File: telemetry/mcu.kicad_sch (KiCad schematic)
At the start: 6 parts, among them J6 ZIO_CN8, J7 ZIO_CN9, J8 ZIO_CN7, J9 ZIO_CN10

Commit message: Updated MCU file to be Nucleo-446RE
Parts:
- removed J6: ZIO_CN8, Connector_PinSocket_2.54mm:PinSocket_2x08_P2.54mm_Vertical, symbol Connector_Generic:Conn_02x08_Odd_Even
- removed J8: ZIO_CN7, Connector_PinSocket_2.54mm:PinSocket_2x10_P2.54mm_Vertical, symbol Connector_Generic:Conn_02x10_Odd_Even
- removed R4, R5: 10k, Resistor_SMD:R_0805_2012Metric_Pad1.20x1.40mm_HandSolder, symbol Device:R_Small
- J7: value ZIO_CN9 -> CN7; symbol Connector_Generic:Conn_02x15_Odd_Even -> Connector_Generic:Conn_02x19_Odd_Even
- J9: value ZIO_CN10 -> CN10; footprint Connector_PinSocket_2.54mm:PinSocket_2x17_P2.54mm_Vertical -> Connector_PinSocket_2.54mm:PinSocket_2x19_P2.54mm_Vertical; symbol Connector_Generic:Conn_02x17_Odd_Even -> Connector_Generic:Conn_02x19_Odd_Even
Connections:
- net APPS_1: no longer names the net of J7.2 (Pin_2)
- net APPS_2: no longer names the net of J7.6 (Pin_6)
- net BPS: no longer names the net of J7.4 (Pin_4)
- net CAN1_RX: no longer names the net of J7.26 (Pin_26)
- net CAN1_TX: no longer names the net of J7.28 (Pin_28)
- net CAN2_TX: no longer names the net of J9.14 (Pin_14)
- net DRS: no longer names the net of J9.30 (Pin_30)
- removed net GND: J7.24 (Pin_24), J9.18 (Pin_18), J9.21 (Pin_21), J9.28 (Pin_28), J9.6 (Pin_6)
- net GPIO_IN_1: no longer names the net of J7.8 (Pin_8)
- net GPIO_IN_2: no longer names the net of J7.10 (Pin_10)
- net GPIO_OUT_1: no longer names the net of J9.5 (Pin_5)
- net GPIO_OUT_2: no longer names the net of J9.7 (Pin_7)
- net GPIO_OUT_3: no longer names the net of J9.9 (Pin_9)
- net RTDI: no longer names the net of J7.12 (Pin_12)
- net RTD_SIREN: no longer names the net of J9.11 (Pin_11)
- net SD: no longer names the net of J7.20 (Pin_20)
- net STATUS: no longer names the net of J9.3 (Pin_3)
- no-connect marks 70 -> 76
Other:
- note added: "3V3"
- note added: "5V"
- note added: "BOOT0"
- note added: "E5V"
- note added: "Nucleo-446 dev board has built in regulator supplied from VIN which provides 3.3V power for rest of circuit, up to 500mA"
- note added: "PA1"
- note added: "PA10"
- note added: "PA11"
- note added: "PA12"
- note added: "PA13"
- note added: "PA14"
- note added: "PA2"
- note added: "PA8"
- note added: "PA9"
- note added: "PB14"
- note added: "PB7"
- note added: "PC1"
- note added: "PC13"
- note added: "PC14"
- note added: "PC15"
- note added: "PC4"
- note added: "PC5"
- note added: "PH0"
- note added: "PH1"
- note added: "STM32 F446RE Nucleo-446"
- note added: "U5V"
- note added: "VBAT"
- note added: "VDD"
- note removed: "+3V3"
- note removed: "+5V"
- note removed: "Nucleo-144 dev board has built in LD1117 regulator supplied from VIN which provides 3.3V power for rest of circuit, up to 800mA"
- note removed: "PB11"
- note removed: "PD0"
- note removed: "PD1"
- note removed: "PD11"
- note removed: "PD12"
- note removed: "PD13"
- note removed: "PD14"
- note removed: "PD15"
- note removed: "PD3"
- note removed: "PD4"
- note removed: "PD5"
- note removed: "PD6"
- note removed: "PD7"
- note removed: "PE0"
- note removed: "PE10"
- note removed: "PE11"
- note removed: "PE13"
- note removed: "PE14"
- note removed: "PE15"
- note removed: "PE2"
- note removed: "PE3"
- note removed: "PE4"
- note removed: "PE5"
- note removed: "PE6"
- note removed: "PE7"
- note removed: "PE8"
- note removed: "PE9"
- note removed: "PF0"
- note removed: "PF1"
- note removed: "PF10"
- note removed: "PF12"
- note removed: "PF13"
- note removed: "PF14"
- note removed: "PF15"
- note removed: "PF2"
- note removed: "PF3"
- note removed: "PF4"
- note removed: "PF5"
- note removed: "PF7"
- note removed: "PF8"
- note removed: "PF9"
- note removed: "PG0"
- note removed: "PG1"
- note removed: "PG14"
- note removed: "PG2"
- note removed: "PG3"
- note removed: "PG9"
- note removed: "STM32 F746ZG Nucleo-144 Zio"
- note removed: "To set bus time constant (RC < 400ns)"

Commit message: nucleo footprint
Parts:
- J7: footprint Connector_PinSocket_2.54mm:PinSocket_2x15_P2.54mm_Vertical -> SUFST:NUCLEO-F446RE-2x19-CON
- J9: footprint Connector_PinSocket_2.54mm:PinSocket_2x19_P2.54mm_Vertical -> SUFST:NUCLEO-F446RE-2x19-CON
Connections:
- net 3V3: now reaches J7.16 (Pin_16)
- no-connect marks 76 -> 75
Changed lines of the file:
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@@
   (no_connect (at 134.62 91.44))
   (no_connect (at 134.62 63.5))
-  (no_connect (at 134.62 78.74))
   (no_connect (at 134.62 81.28))
   (no_connect (at 134.62 83.82))
@@
     (effects (font (size 1.27 1.27)) (justify left bottom))
   )
+  (hierarchical_label "3V3" (shape output) (at 134.62 78.74 0)
+    (effects (font (size 1.27 1.27)) (justify left))
+  )
   (symbol (lib_id "Connector_Generic:Conn_02x19_Odd_Even") (at 170.18 83.82 0) (unit 1)
     (in_bom yes) (on_board yes)
-    (property "Reference" "J9" (id 0) (at 171.45 113.03 0)
-      (effects (font (size 1.27 1.27)) hide)
-    )
+    (property "Reference" "J9" (id 0) (at 171.45 113.03 0))
     (property "Value" "CN10" (id 1) (at 171.45 110.49 0))
-    (property "Footprint" "Connector_PinSocket_2.54mm:PinSocket_2x19_P2.54mm_Vertical" (id 2) (at 170.18 83.82 0)
+    (property "Footprint" "SUFST:NUCLEO-F446RE-2x19-CON" (id 2) (at 170.18 83.82 0)
       (effects (font (size 1.27 1.27)) hide)
     )
@@
   (symbol (lib_id "Connector_Generic:Conn_02x19_Odd_Even") (at 115.57 83.82 0) (unit 1)
     (in_bom yes) (on_board yes)
-    (property "Reference" "J7" (id 0) (at 116.84 113.03 0)
+    (property "Reference" "J7" (id 0) (at 116.84 113.03 0))
+    (property "Value" "CN7" (id 1) (at 116.84 110.49 0))
+    (property "Footprint" "SUFST:NUCLEO-F446RE-2x19-CON" (id 2) (at 115.57 83.82 0)
       (effects (font (size 1.27 1.27)) hide)
     )
-    (property "Value" "CN7" (id 1) (at 116.84 110.49 0))
-    (property "Footprint" "Connector_PinSocket_2.54mm:PinSocket_2x15_P2.54mm_Vertical" (id 2) (at 115.57 83.82 0)
-      (effects (font (size 1.27 1.27)) hide)
-    )

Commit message: components org
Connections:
- net GND: now reaches J9.20 (Pin_20)
- net GND: now also J7.19 (Pin_19), J7.20 (Pin_20), J7.22 (Pin_22), J7.8 (Pin_8), J9.9 (Pin_9)
- net VIN: now reaches J7.24 (Pin_24)
- no-connect marks 75 -> 68
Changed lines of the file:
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@@
     (comment 3 "Max O'Brien")
+  )
+  (junction (at 146.05 68.58) (diameter 0) (color 0 0 0 0)
+  )
+  (junction (at 146.05 86.36) (diameter 0) (color 0 0 0 0)
   )
   (no_connect (at 100.33 81.28))
@@
   (no_connect (at 100.33 106.68))
   (no_connect (at 100.33 60.96))
-  (no_connect (at 100.33 83.82))
   (no_connect (at 156.21 86.36))
   (no_connect (at 156.21 88.9))
@@
   (no_connect (at 156.21 76.2))
   (no_connect (at 156.21 73.66))
-  (no_connect (at 156.21 71.12))
   (no_connect (at 156.21 81.28))
   (no_connect (at 100.33 88.9))
@@
   (no_connect (at 134.62 96.52))
   (no_connect (at 134.62 99.06))
-  (no_connect (at 134.62 88.9))
-  (no_connect (at 134.62 86.36))
   (no_connect (at 134.62 91.44))
   (no_connect (at 134.62 63.5))
   (no_connect (at 134.62 81.28))
-  (no_connect (at 134.62 83.82))
   (no_connect (at 134.62 76.2))
   (no_connect (at 134.62 66.04))
   (no_connect (at 134.62 73.66))
-  (no_connect (at 134.62 68.58))
   (no_connect (at 134.62 71.12))
   (no_connect (at 187.96 73.66))
   (no_connect (at 187.96 86.36))
-  (no_connect (at 187.96 83.82))
   (no_connect (at 187.96 81.28))
   (no_connect (at 187.96 78.74))
   (no_connect (at 187.96 63.5))
-  (wire (pts (xy 156.21 71.12) (xy 165.1 71.12))
+  (wire (pts (xy 151.13 71.12) (xy 165.1 71.12))
     (stroke (width 0) (type default) (color 0 0 0 0))
   )
@@
     (stroke (width 0) (type default) (color 0 0 0 0))
   )
-  (wire (pts (xy 177.8 83.82) (xy 187.96 83.82))
+  (wire (pts (xy 177.8 83.82) (xy 195.58 83.82))
     (stroke (width 0) (type default) (color 0 0 0 0))
   )
@@
     (stroke (width 0) (type default) (color 0 0 0 0))
   )
+  (wire (pts (xy 195.58 83.82) (xy 195.58 86.36))
+    (stroke (width 0) (type default) (color 0 0 0 0))
+  )
   (wire (pts (xy 123.19 99.06) (xy 134.62 99.06))
     (stroke (width 0) (type default) (color 0 0 0 0))
@@
     (stroke (width 0) (type default) (color 0 0 0 0))
   )
-  (wire (pts (xy 123.19 68.58) (xy 134.62 68.58))
+  (wire (pts (xy 123.19 68.58) (xy 146.05 68.58))
     (stroke (width 0) (type default) (color 0 0 0 0))
   )
@@
     (stroke (width 0) (type default) (color 0 0 0 0))
   )
-  (wire (pts (xy 100.33 83.82) (xy 110.49 83.82))
+  (wire (pts (xy 90.17 83.82) (xy 110.49 83.82))
     (stroke (width 0) (type default) (color 0 0 0 0))
   )
@@
     (stroke (width 0) (type default) (color 0 0 0 0))
   )
+  (wire (pts (xy 146.05 68.58) (xy 146.05 69.85))
+    (stroke (width 0) (type default) (color 0 0 0 0))
+  )
   (wire (pts (xy 177.8 86.36) (xy 187.96 86.36))
     (stroke (width 0) (type default) (color 0 0 0 0))
@@
     (stroke (width 0) (type default) (color 0 0 0 0))
   )
+  (wire (pts (xy 146.05 83.82) (xy 146.05 86.36))
+    (stroke (width 0) (type default) (color 0 0 0 0))
+  )
   (wire (pts (xy 177.8 78.74) (xy 187.96 78.74))
     (stroke (width 0) (type default) (color 0 0 0 0))
@@
     (stroke (width 0) (type default) (color 0 0 0 0))
   )
+  (wire (pts (xy 151.13 71.12) (xy 151.13 68.58))
+    (stroke (width 0) (type default) (color 0 0 0 0))
+  )
   (wire (pts (xy 123.19 66.04) (xy 134.62 66.04))
     (stroke (width 0) (type default) (color 0 0 0 0))
@@
     (stroke (width 0) (type default) (color 0 0 0 0))
   )
-  (wire (pts (xy 123.19 86.36) (xy 134.62 86.36))
+  (wire (pts (xy 123.19 86.36) (xy 146.05 86.36))
     (stroke (width 0) (type default) (color 0 0 0 0))
   )
@@
     (stroke (width 0) (type default) (color 0 0 0 0))
   )
+  (wire (pts (xy 146.05 87.63) (xy 146.05 86.36))
+    (stroke (width 0) (type default) (color 0 0 0 0))
+  )
   (wire (pts (xy 123.19 96.52) (xy 134.62 96.52))
     (stroke (width 0) (type default) (color 0 0 0 0))
@@
     (stroke (width 0) (type default) (color 0 0 0 0))
   )
+  (wire (pts (xy 90.17 83.82) (xy 90.17 85.09))
+    (stroke (width 0) (type default) (color 0 0 0 0))
+  )
   (wire (pts (xy 177.8 101.6) (xy 187.96 101.6))
     (stroke (width 0) (type default) (color 0 0 0 0))
@@
     (stroke (width 0) (type default) (color 0 0 0 0))
   )
+  (wire (pts (xy 151.13 68.58) (xy 146.05 68.58))
+    (stroke (width 0) (type default) (color 0 0 0 0))
+  )
   (wire (pts (xy 123.19 63.5) (xy 134.62 63.5))
     (stroke (width 0) (type default) (color 0 0 0 0))
   )
-  (wire (pts (xy 123.19 83.82) (xy 134.62 83.82))
+  (wire (pts (xy 123.19 83.82) (xy 146.05 83.82))
     (stroke (width 0) (type default) (color 0 0 0 0))
   )
@@
     (effects (font (size 1.27 1.27)) (justify left bottom))
   )
+  (hierarchical_label "VIN" (shape output) (at 134.62 88.9 0)
+    (effects (font (size 1.27 1.27)) (justify left))
+  )
   (hierarchical_label "3V3" (shape output) (at 134.62 78.74 0)
     (effects (font (size 1.27 1.27)) (justify left))
   )
+  (symbol (lib_id "power:GND") (at 146.05 87.63 0) (unit 1)
+    (in_bom yes) (on_board yes)
+    (property "Reference" "#PWR0114" (id 0) (at 146.05 93.98 0)
+      (effects (font (size 1.27 1.27)) hide)
+    )
+    (property "Value" "GND" (id 1) (at 146.05 91.44 0))
+    (property "Footprint" "" (id 2) (at 146.05 87.63 0)
+      (effects (font (size 1.27 1.27)) hide)
+    )
+    (property "Datasheet" "" (id 3) (at 146.05 87.63 0)
+      (effects (font (size 1.27 1.27)) hide)
+    )
+    (pin "1")
+  )
+  (symbol (lib_id "power:GND") (at 90.17 85.09 0) (unit 1)
+    (in_bom yes) (on_board yes)
+    (property "Reference" "#PWR0115" (id 0) (at 90.17 91.44 0)
+      (effects (font (size 1.27 1.27)) hide)
+    )
+    (property "Value" "GND" (id 1) (at 90.17 88.9 0))
+    (property "Footprint" "" (id 2) (at 90.17 85.09 0)
+      (effects (font (size 1.27 1.27)) hide)
+    )
+    (property "Datasheet" "" (id 3) (at 90.17 85.09 0)
+      (effects (font (size 1.27 1.27)) hide)
+    )
+    (pin "1")
+  )
+  (symbol (lib_id "power:GND") (at 146.05 69.85 0) (unit 1)
+    (in_bom yes) (on_board yes)
+    (property "Reference" "#PWR0113" (id 0) (at 146.05 76.2 0)
+      (effects (font (size 1.27 1.27)) hide)
+    )
+    (property "Value" "GND" (id 1) (at 146.05 73.66 0))
+    (property "Footprint" "" (id 2) (at 146.05 69.85 0)
+      (effects (font (size 1.27 1.27)) hide)
+    )
+    (property "Datasheet" "" (id 3) (at 146.05 69.85 0)
+      (effects (font (size 1.27 1.27)) hide)
+    )
+    (pin "1")
+  )
+  (symbol (lib_id "power:GND") (at 195.58 86.36 0) (unit 1)
+    (in_bom yes) (on_board yes)
+    (property "Reference" "#PWR0112" (id 0) (at 195.58 92.71 0)
+      (effects (font (size 1.27 1.27)) hide)
+    )
+    (property "Value" "GND" (id 1) (at 195.58 90.17 0))
+    (property "Footprint" "" (id 2) (at 195.58 86.36 0)
+      (effects (font (size 1.27 1.27)) hide)
+    )
+    (property "Datasheet" "" (id 3) (at 195.58 86.36 0)
+      (effects (font (size 1.27 1.27)) hide)
+    )
+    (pin "1")
+  )
   (symbol (lib_id "Connector_Generic:Conn_02x19_Odd_Even") (at 170.18 83.82 0) (unit 1)

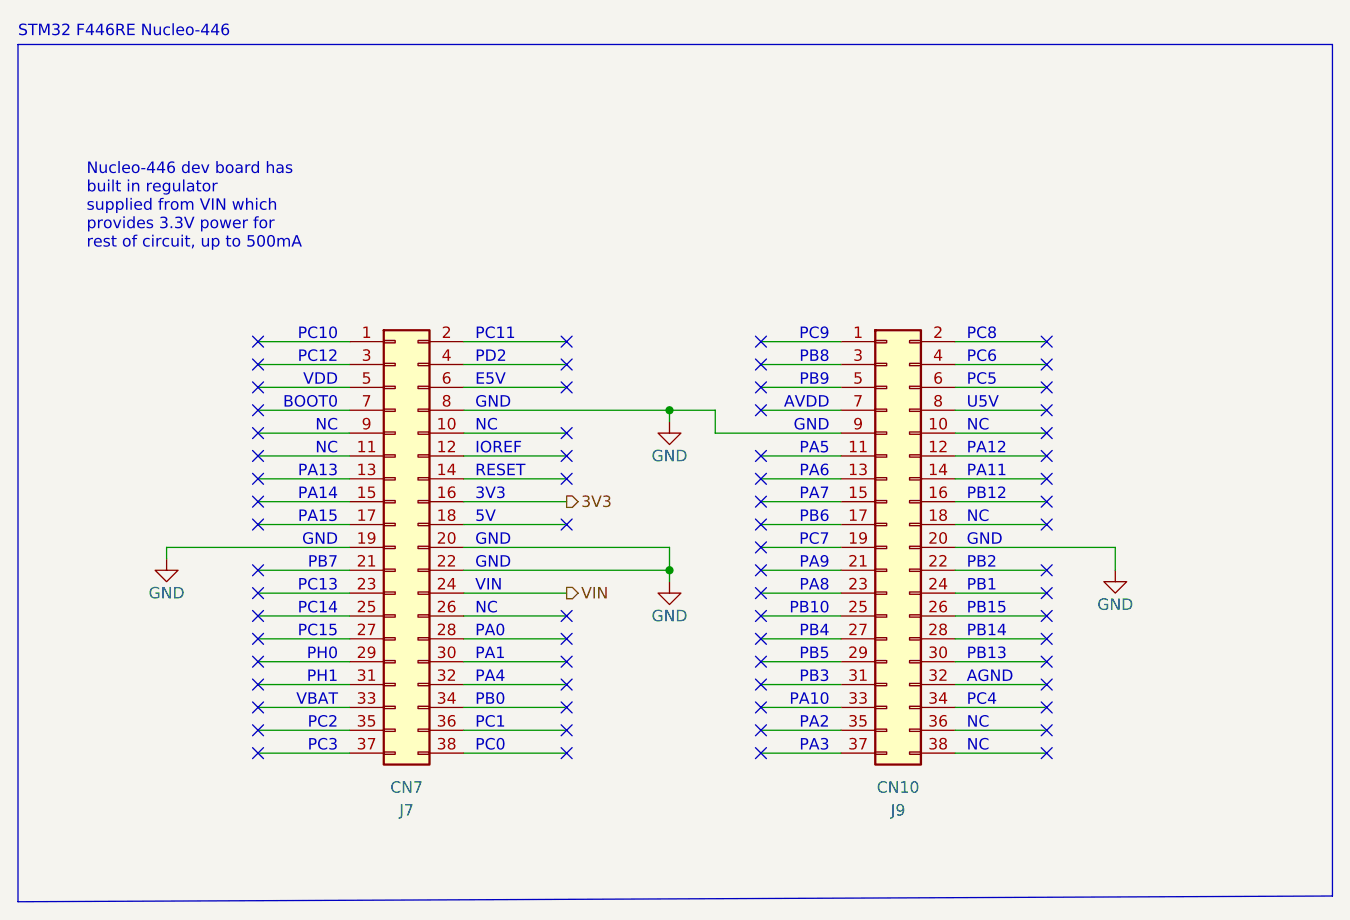
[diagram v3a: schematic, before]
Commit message: added MCU pins and GPS
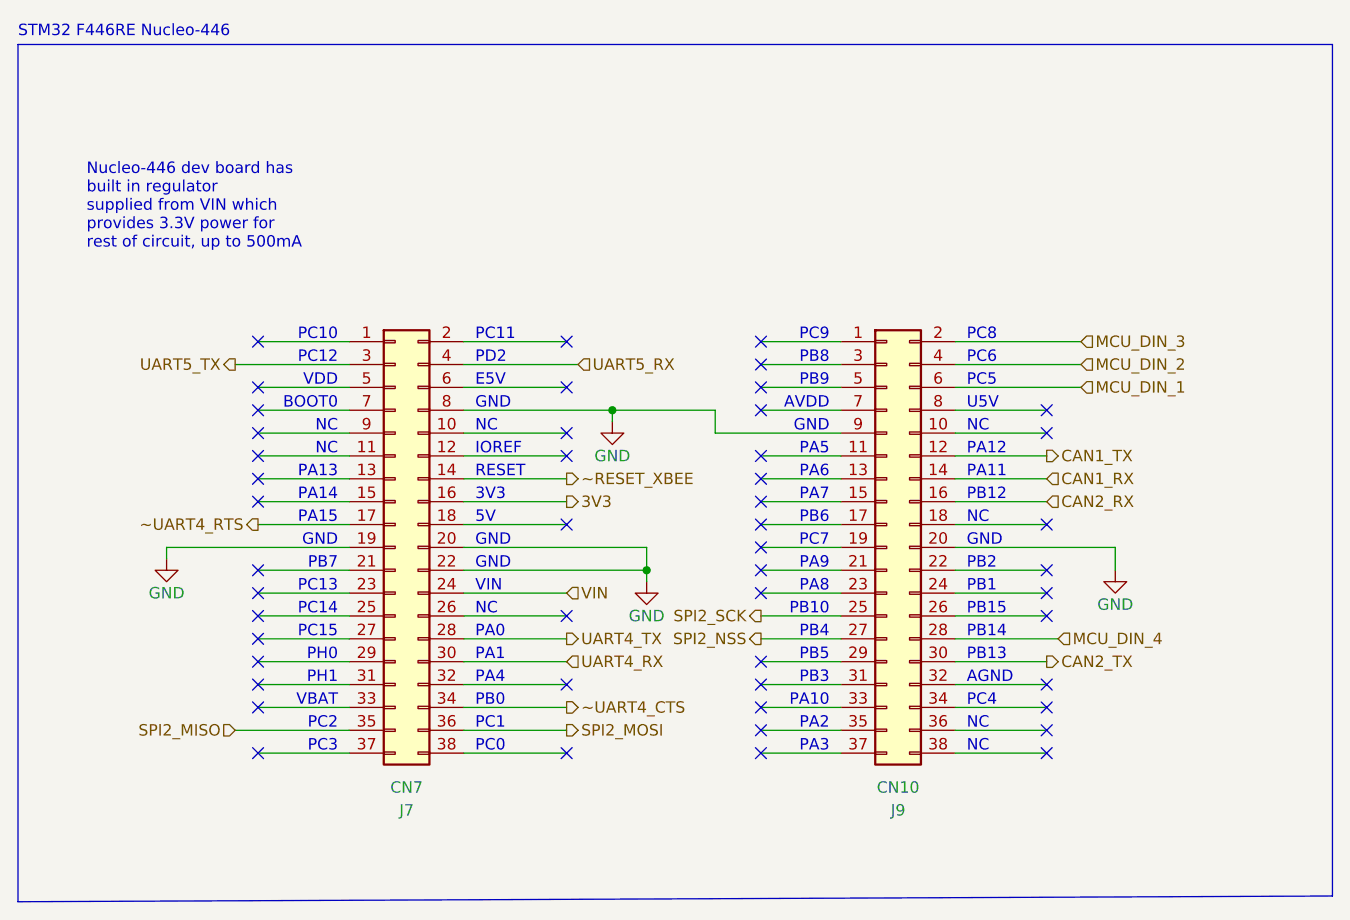
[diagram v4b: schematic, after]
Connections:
- net CAN1_TX: now reaches J9.12 (Pin_12)
- net CAN1_RX: now reaches J9.14 (Pin_14)
- net CAN2_RX: now reaches J9.16 (Pin_16)
- net MCU_DIN_3: now reaches J9.2 (Pin_2)
- net SPI2_SCK: now reaches J9.25 (Pin_25)
- net SPI2_NSS: now reaches J9.27 (Pin_27)
- net MCU_DIN_4: now reaches J9.28 (Pin_28)
- net CAN2_TX: now reaches J9.30 (Pin_30)
- net MCU_DIN_2: now reaches J9.4 (Pin_4)
- net MCU_DIN_1: now reaches J9.6 (Pin_6)
- net ~RESET_XBEE: now reaches J7.14 (Pin_14)
- net ~UART4_RTS: now reaches J7.17 (Pin_17)
- net UART4_TX: now reaches J7.28 (Pin_28)
- net UART5_TX: now reaches J7.3 (Pin_3)
- net UART4_RX: now reaches J7.30 (Pin_30)
- net ~UART4_CTS: now reaches J7.34 (Pin_34)
- net SPI2_MISO: now reaches J7.35 (Pin_35)
- net SPI2_MOSI: now reaches J7.36 (Pin_36)
- net UART5_RX: now reaches J7.4 (Pin_4)
- no-connect marks 68 -> 49

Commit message: routing
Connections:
- net MCU_DIN_4: now also J9.3 (Pin_3); no longer J9.28 (Pin_28)
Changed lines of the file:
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@@
   (no_connect (at 156.21 76.2))
   (no_connect (at 156.21 66.04))
-  (no_connect (at 156.21 63.5))
   (no_connect (at 100.33 96.52))
   (no_connect (at 100.33 101.6))
@@
   (no_connect (at 156.21 106.68))
   (no_connect (at 100.33 78.74))
+  (no_connect (at 187.96 93.98))
   (no_connect (at 100.33 66.04))
   (no_connect (at 156.21 83.82))
@@
     (stroke (width 0) (type default) (color 0 0 0 0))
   )
-  (wire (pts (xy 156.21 63.5) (xy 165.1 63.5))
+  (wire (pts (xy 152.4 63.5) (xy 165.1 63.5))
     (stroke (width 0) (type default) (color 0 0 0 0))
   )
@@
     (stroke (width 0) (type default) (color 0 0 0 0))
   )
+  (wire (pts (xy 152.4 63.5) (xy 152.4 66.04))
+    (stroke (width 0) (type default) (color 0 0 0 0))
+  )
   (wire (pts (xy 123.19 88.9) (xy 134.62 88.9))
     (stroke (width 0) (type default) (color 0 0 0 0))
@@
     (stroke (width 0) (type default) (color 0 0 0 0))
   )
-  (wire (pts (xy 177.8 93.98) (xy 189.23 93.98))
-    (stroke (width 0) (type default) (color 0 0 0 0))
-  )
   (wire (pts (xy 100.33 93.98) (xy 110.49 93.98))
     (stroke (width 0) (type default) (color 0 0 0 0))
@@
   )
   (wire (pts (xy 123.19 68.58) (xy 139.7 68.58))
+    (stroke (width 0) (type default) (color 0 0 0 0))
+  )
+  (wire (pts (xy 177.8 93.98) (xy 187.96 93.98))
     (stroke (width 0) (type default) (color 0 0 0 0))
   )
@@
     (effects (font (size 1.27 1.27)) (justify left))
   )
-  (hierarchical_label "MCU_DIN_4" (shape input) (at 189.23 93.98 0)
-    (effects (font (size 1.27 1.27)) (justify left))
-  )
   (hierarchical_label "SPI2_MISO" (shape input) (at 97.79 104.14 180)
     (effects (font (size 1.27 1.27)) (justify right))
@@
     (effects (font (size 1.27 1.27)) (justify left))
   )
+  (hierarchical_label "MCU_DIN_4" (shape input) (at 152.4 66.04 180)
+    (effects (font (size 1.27 1.27)) (justify right))
+  )
   (hierarchical_label "~RESET_XBEE" (shape output) (at 134.62 76.2 0)

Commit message: chore: add sheet information
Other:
- company: SUFST -> SUFST - Southampton University Formula Student Team
- title: VCU -> On-Car Telemetry
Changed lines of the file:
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@@
 (kicad_sch (version 20211123) (generator eeschema)
-  (paper "A3")
+  (paper "A4")
   (title_block
-    (title "VCU")
-    (date "2022-11-20")
-    (rev "1.0")
-    (company "SUFST")
+    (title "On-Car Telemetry")
+    (date "2023-03-31")
+    (rev "1.0.0")
+    (company "SUFST - Southampton University Formula Student Team")
     (comment 1 "STAG 9")
-    (comment 2 "Tim Brewis")
-    (comment 3 "Max O'Brien")
+    (comment 2 "Esteban Norena")
+    (comment 3 "Tim Brewis")
   )
   (junction (at 139.7 68.58) (diameter 0) (color 0 0 0 0)
